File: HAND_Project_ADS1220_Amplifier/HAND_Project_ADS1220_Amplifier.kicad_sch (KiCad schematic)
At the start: 12 parts, among them J1 Screw_Terminal_01x04, J2 Conn_01x05_Pin, J7 Conn_01x04_Pin, U1 ADS1220IPWR

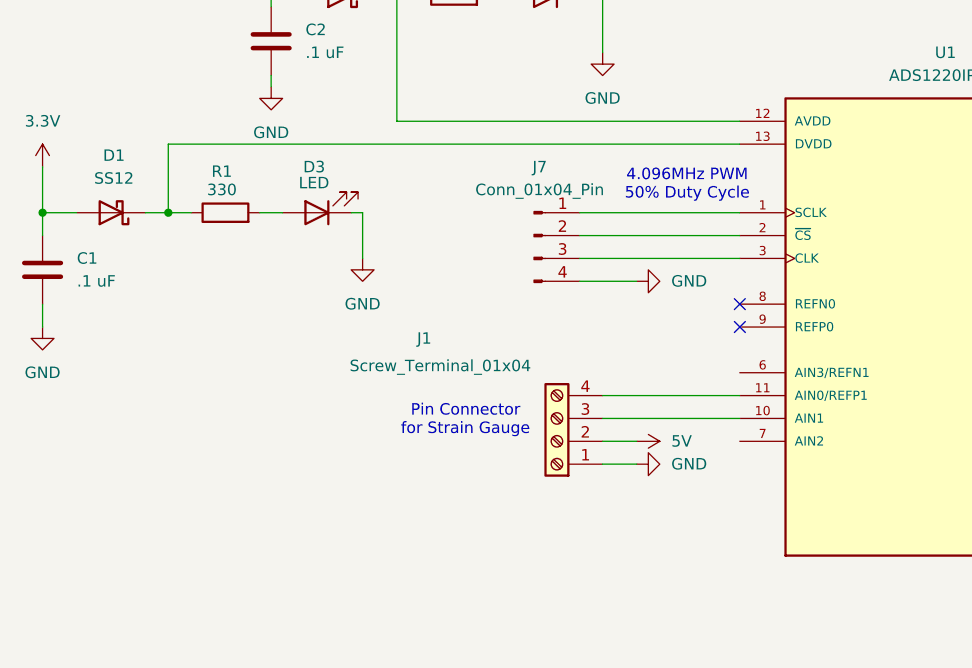
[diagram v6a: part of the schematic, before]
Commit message: Components Update
Update 1: 2x LPF RC filters added for both Analog Signals from the J1 screw into the ADS

Update 2: 1x Power Connector pin for 5V and GND added as suggested by Luke
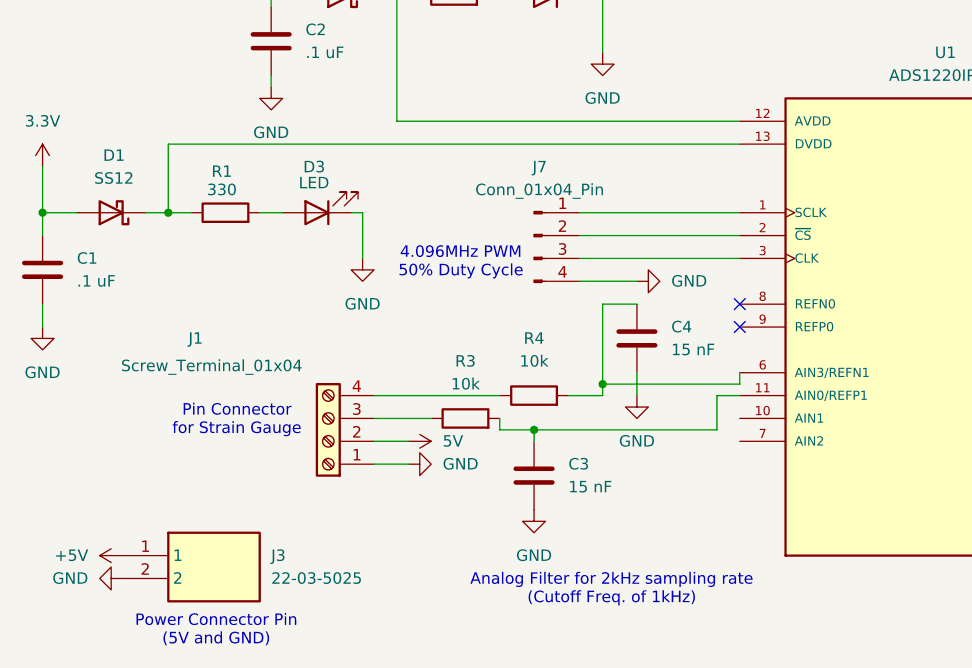
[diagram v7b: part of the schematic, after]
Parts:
- added C3, C4: 15 nF, Capacitor_SMD:C_0603_1608Metric_Pad1.08x0.95mm_HandSolder, symbol Device:C
- added J3: 22-03-5025, SHDR2W70P0X250_1X2_740X490X590P, symbol SamacSys_Parts:22-03-5025
- added R3, R4: 10k, Resistor_SMD:R_0603_1608Metric_Pad0.98x0.95mm_HandSolder, symbol Device:R
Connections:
- net GND: now also C3.2, C4.2, J3.2
- net at J1.3 (Pin_3): now also R3.1; no longer U1.10 (AIN1)
- net at U1.11 (AIN0/REFP1): now also C3.1, R3.2; no longer J1.4 (Pin_4)
- net at U1.6 (AIN3/REFN1): now also C4.1, R4.2
- new net: J1.4 (Pin_4), R4.1
- new net +5V: J3.1
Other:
- note added: "Analog Filter for 2kHz sampling rate (Cutoff Freq. of 1kHz)"
- note added: "Power Connector Pin (5V and GND)"
- moved on the sheet: J1

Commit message: Eric's PCB (without teensy integration)
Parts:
- removed J3: 22-03-5025, SHDR2W70P0X250_1X2_740X490X590P, symbol SamacSys_Parts:22-03-5025
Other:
- note removed: "Power Connector Pin (5V and GND)"
